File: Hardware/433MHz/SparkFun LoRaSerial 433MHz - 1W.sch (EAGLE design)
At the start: 96 parts, among them J1 QWIIC_RIGHT_ANGLE, J3 USB C, J4 JTAG, Q1 20V/0.2A/8MHz/1.2Ω/1Vth, Q2 20V/0.2A/8MHz/1.2Ω/1Vth, Q3 600mA/40V, Q4 600mA/40V, Q5 600mA/40V, Q6 600mA/40V, Q8 20V/4.2A/52mΩ/1.4W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

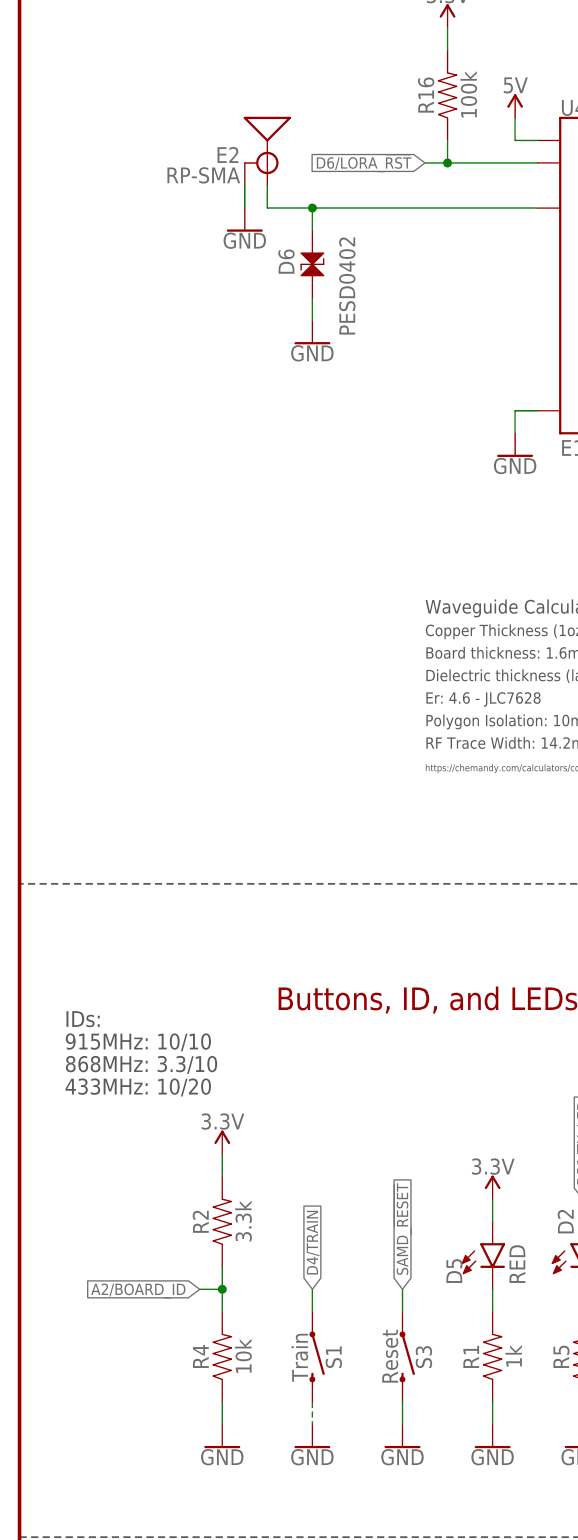
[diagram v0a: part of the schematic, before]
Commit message: Add 433MHz and 868MHz designs
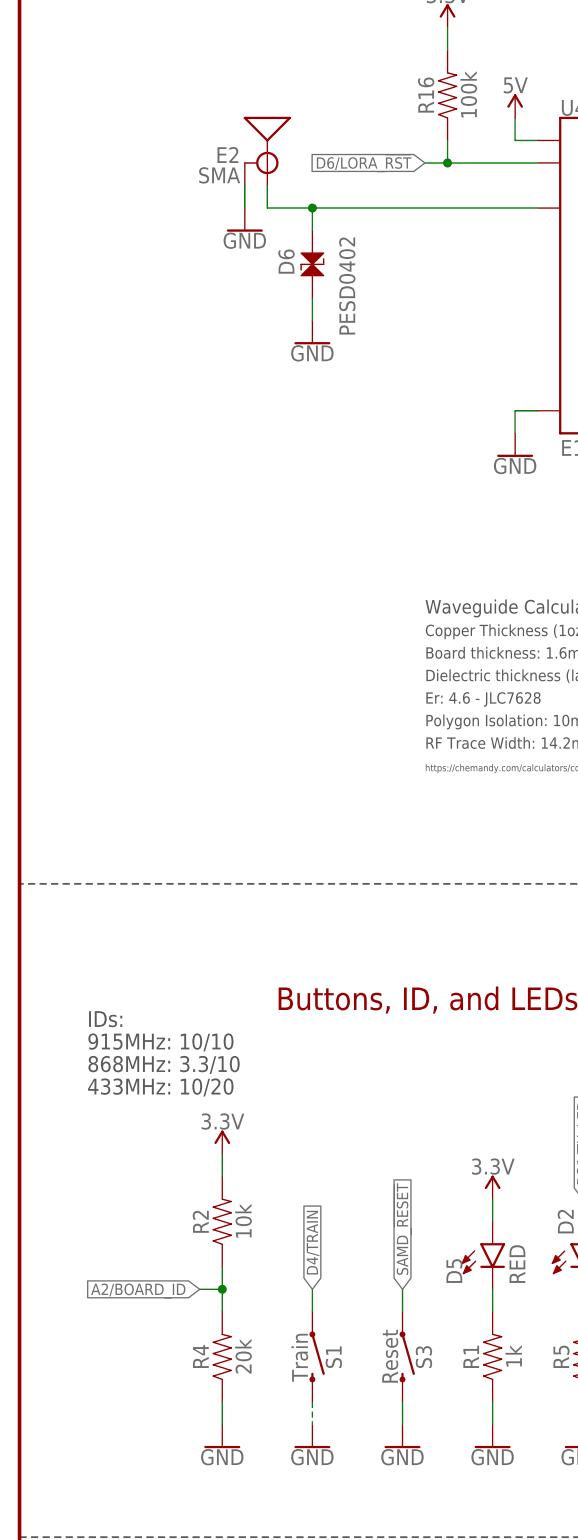
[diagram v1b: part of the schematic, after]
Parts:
- E2: value RP-SMA -> SMA; device SparkFun-RF:ANTENNA-SMA-GROUNDEDEDGE_RPSMA -> SparkFun-RF:ANTENNA-SMA-GROUNDEDEDGE_SMA
- R2: value 3.3k -> 10k; device SparkFun-Resistors:3.3KOHM-0603-1/10W-1% -> SparkFun-Resistors:10KOHM-0603-1/10W-1%
- R4: value 10k -> 20k; device SparkFun-Resistors:10KOHM-0603-1/10W-1% -> SparkFun-Resistors:20KOHM-0603-1/10W-1%
- U4: device SparkFun-RF:LORA-E19868MHZ -> SparkFun-RF:LORA-E19433MHZ
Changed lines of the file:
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@@
 <part name="LOGO4" library="SparkFun-Aesthetics" deviceset="OSHW-LOGO" device="MINI" value="OSHW-LOGOMINI"/>
 <part name="GND31" library="SparkFun-PowerSymbols" deviceset="GND" device=""/>
-<part name="U4" library="SparkFun-RF" deviceset="LORA-E19" device="868MHZ" value="E19-915M30S"/>
+<part name="U4" library="SparkFun-RF" deviceset="LORA-E19" device="433MHZ" value="E19-915M30S"/>
 <part name="R16" library="SparkFun-Resistors" deviceset="100KOHM" device="-0603-1/10W-1%" value="100k"/>
 <part name="SUPPLY12" library="SparkFun-PowerSymbols" deviceset="3.3V" device=""/>
@@
 <part name="SUPPLY13" library="SparkFun-PowerSymbols" deviceset="5V" device=""/>
 <part name="GND4" library="SparkFun-PowerSymbols" deviceset="GND" device=""/>
-<part name="R2" library="SparkFun-Resistors" deviceset="3.3KOHM" device="-0603-1/10W-1%" value="3.3k"/>
-<part name="R4" library="SparkFun-Resistors" deviceset="10KOHM" device="-0603-1/10W-1%" value="10k"/>
+<part name="R2" library="SparkFun-Resistors" deviceset="10KOHM" device="-0603-1/10W-1%" value="10k"/>
+<part name="R4" library="SparkFun-Resistors" deviceset="20KOHM" device="-0603-1/10W-1%" value="20k"/>
 <part name="SUPPLY7" library="SparkFun-PowerSymbols" deviceset="3.3V" device=""/>
 <part name="GND3" library="SparkFun-PowerSymbols" deviceset="GND" device=""/>
@@
 <part name="SUPPLY9" library="SparkFun-PowerSymbols" deviceset="3.3V" device=""/>
 <part name="JP9" library="SparkFun-Jumpers" deviceset="JUMPER-SMT_3_2-NC_TRACE" device="_SILK" package3d_urn="urn:adsk.eagle:package:39289/1" value="JUMPER-SMT_3_2-NC_TRACE_SILK"/>
-<part name="E2" library="SparkFun-RF" deviceset="ANTENNA-SMA-GROUNDED" device="EDGE_RPSMA" value="RP-SMA"/>
+<part name="E2" library="SparkFun-RF" deviceset="ANTENNA-SMA-GROUNDED" device="EDGE_SMA" value="SMA"/>
 <part name="S1" library="SparkFun-Switches" deviceset="MOMENTARY-SWITCH-SPST" device="-SMD-RIGHT-ANGLE" value="Train"/>
 <part name="GND9" library="SparkFun-PowerSymbols" deviceset="GND" device=""/>
@@
 <wire x1="88.9" y1="76.2" x2="88.9" y2="149.86" width="0.2032" layer="97" style="longdash"/>
 <wire x1="66.04" y1="0" x2="66.04" y2="76.2" width="0.2032" layer="97" style="longdash"/>
-<text x="5.08" y="134.62" size="1.778" layer="97" align="center-left">IDs:</text>
-<text x="5.08" y="132.08" size="1.778" layer="97" align="center-left">915MHz: 10/10</text>
-<text x="5.08" y="129.54" size="1.778" layer="97" align="center-left">868MHz: 3.3/10</text>
-<text x="5.08" y="127" size="1.778" layer="97" align="center-left">433MHz: 10/20</text>
+<text x="7.62" y="134.62" size="1.778" layer="97" align="center-left">IDs:</text>
+<text x="7.62" y="132.08" size="1.778" layer="97" align="center-left">915MHz: 10/10</text>
+<text x="7.62" y="129.54" size="1.778" layer="97" align="center-left">868MHz: 3.3/10</text>
+<text x="7.62" y="127" size="1.778" layer="97" align="center-left">433MHz: 10/20</text>
 </plain>
 <instances>
@@
 </sheet>
 </sheets>
-<errors>
-</errors>
 </schematic>
 </drawing>

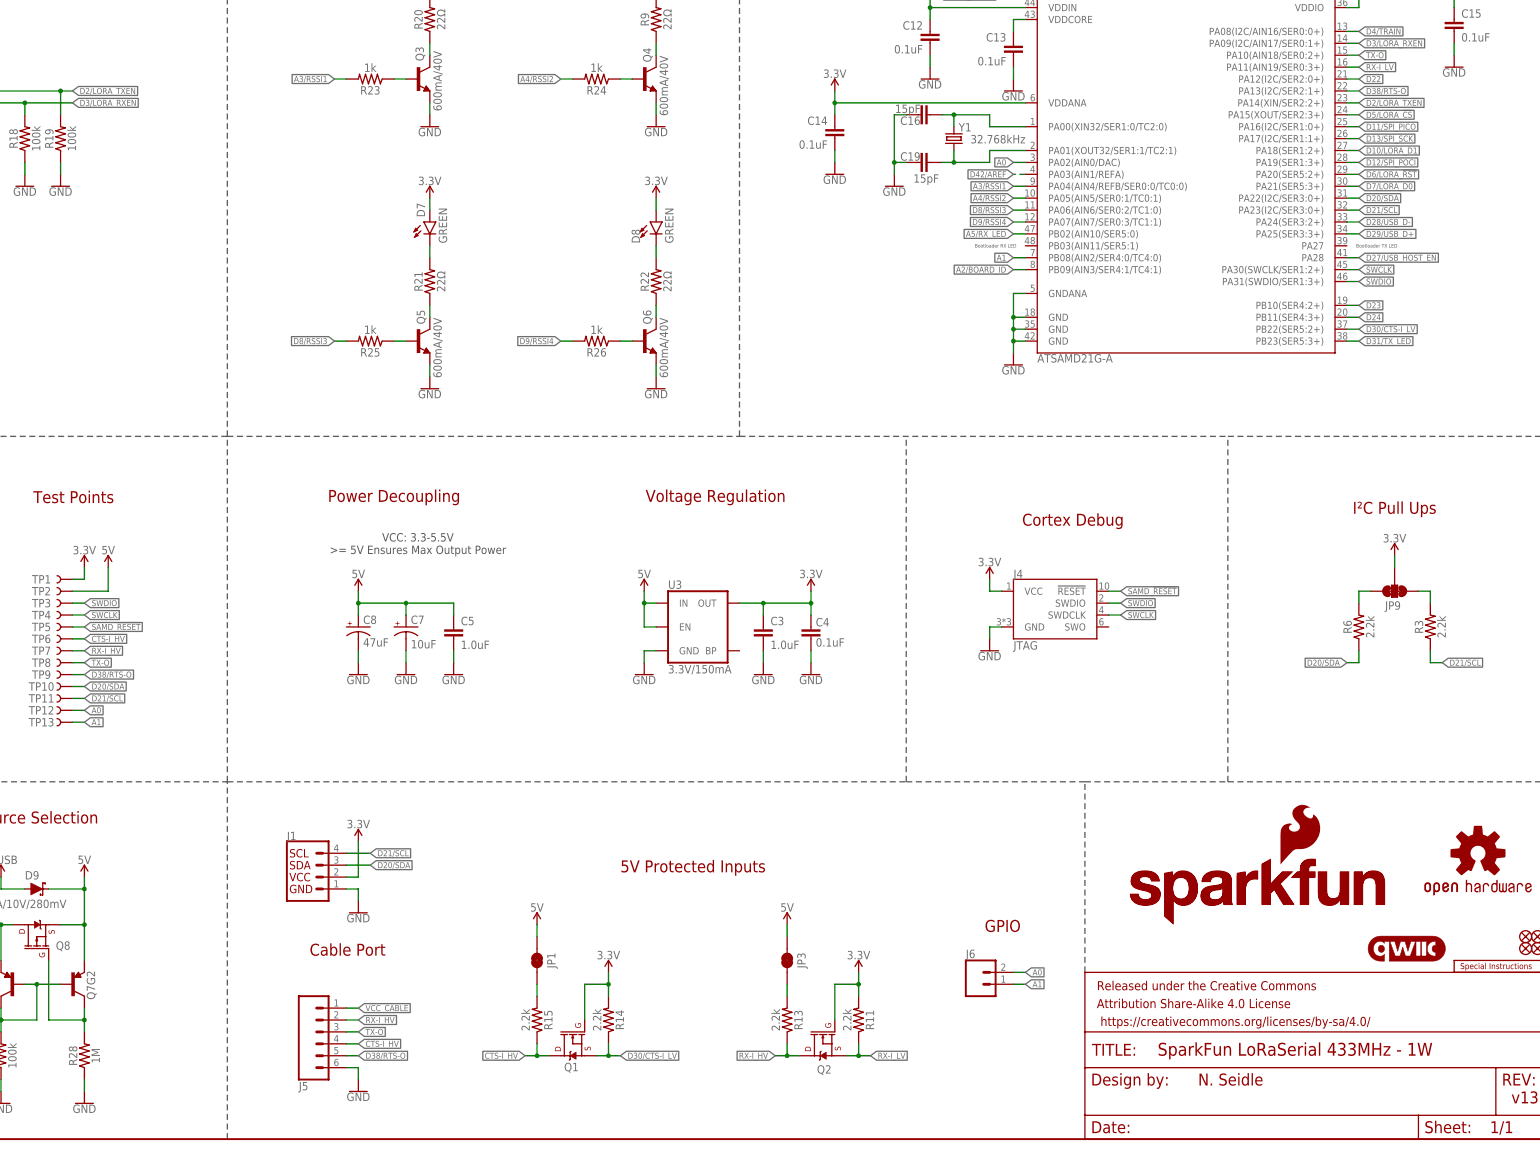
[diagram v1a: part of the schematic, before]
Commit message: Update schematics with flow control notes
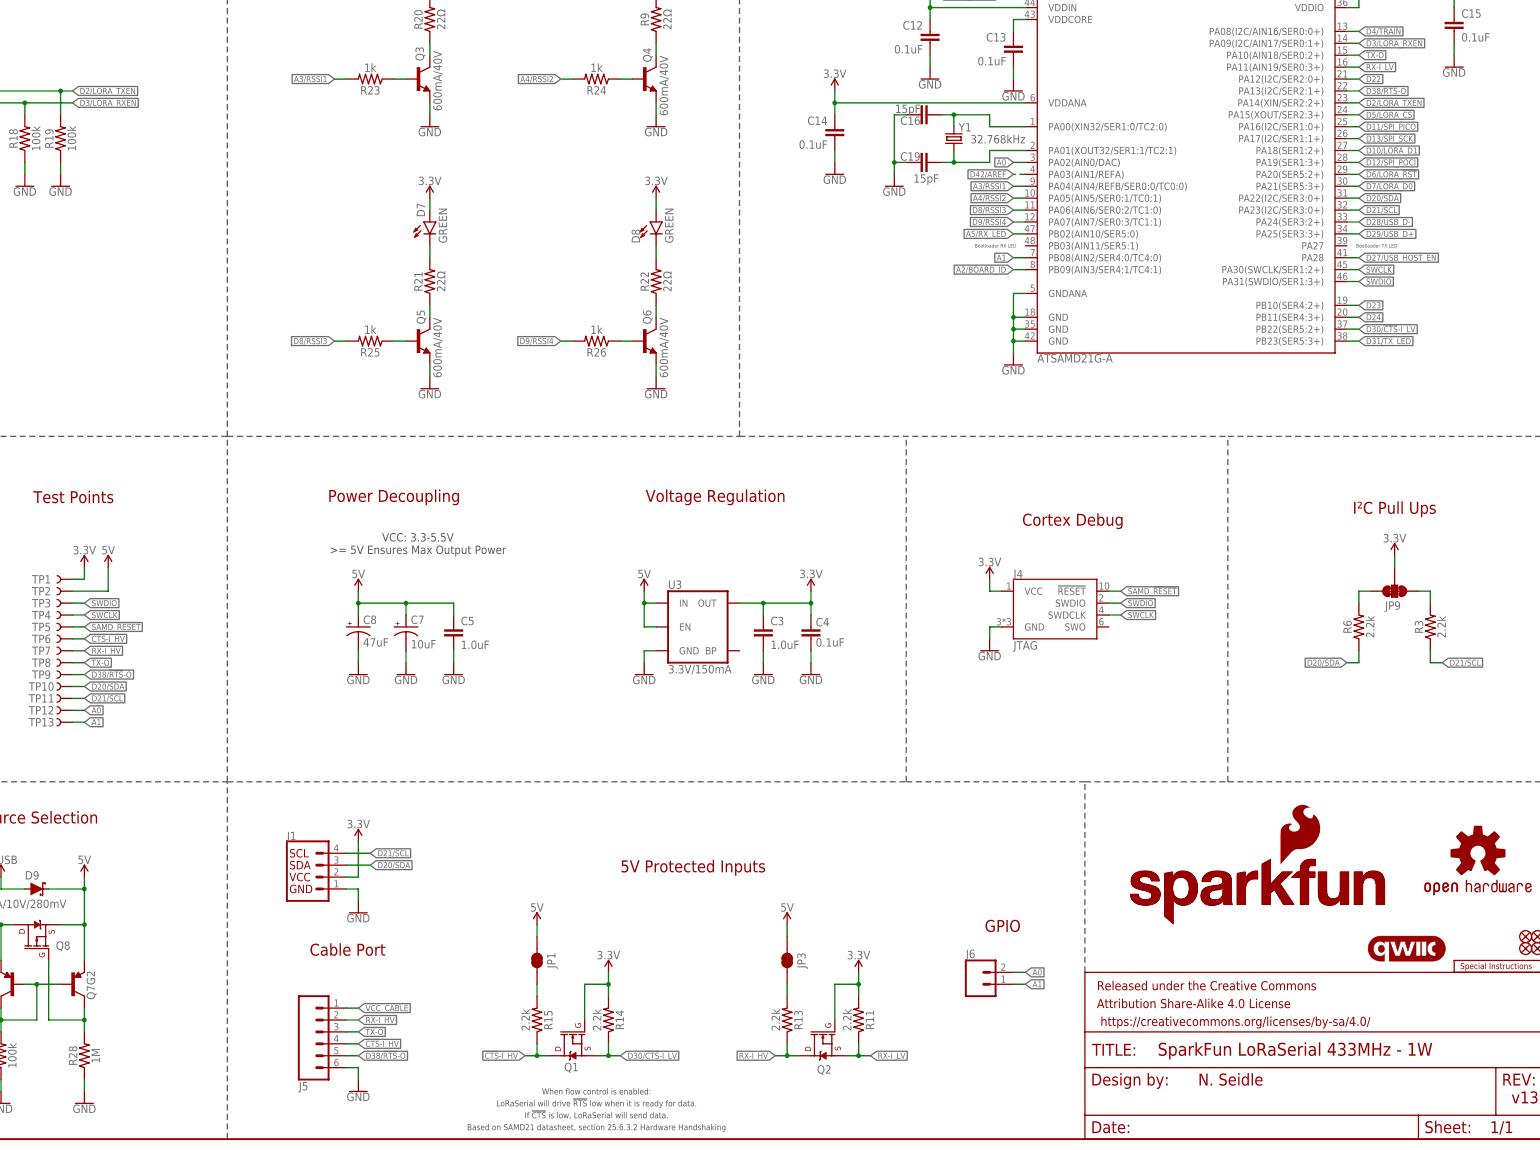
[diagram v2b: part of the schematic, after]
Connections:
- net CTS-I_HV renamed !CTS!-I_HV
- net D30/CTS-I_LV renamed D30/!CTS!-I_LV
- net D38/RTS-O renamed D38/!RTS!-O
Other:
- note added: "Based on SAMD21 datasheet, section 25.6.3.2 Hardware Handshaking"
- note added: "If !CTS! is low, LoRaSerial will send data."
- note added: "LoRaSerial will drive !RTS! low when it is ready for data."
- note added: "When flow control is enabled:"
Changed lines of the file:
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@@
 <text x="7.62" y="129.54" size="1.778" layer="97" align="center-left">868MHz: 3.3/10</text>
 <text x="7.62" y="127" size="1.778" layer="97" align="center-left">433MHz: 10/20</text>
+<text x="226.06" y="7.62" size="1.27" layer="97" font="vector" align="center">LoRaSerial will drive !RTS! low when it is ready for data.</text>
+<text x="226.06" y="5.08" size="1.27" layer="97" font="vector" align="center">If !CTS! is low, LoRaSerial will send data.</text>
+<text x="226.06" y="2.54" size="1.27" layer="97" font="vector" align="center">Based on SAMD21 datasheet, section 25.6.3.2 Hardware Handshaking</text>
+<text x="226.06" y="10.16" size="1.27" layer="97" font="vector" align="center">When flow control is enabled:</text>
 </plain>
 <instances>
@@
 </segment>
 </net>
-<net name="D30/CTS-I_LV" class="0">
+<net name="D30/!CTS!-I_LV" class="0">
 <segment>
 <pinref part="U2" gate="G$1" pin="PB22(SER5:2+)"/>
@@
 </segment>
 </net>
-<net name="D38/RTS-O" class="0">
+<net name="D38/!RTS!-O" class="0">
 <segment>
 <pinref part="U2" gate="G$1" pin="PA13(I2C/SER2:1+)"/>
@@
 </segment>
 </net>
-<net name="CTS-I_HV" class="0">
+<net name="!CTS!-I_HV" class="0">
 <segment>
 <label x="175.26" y="20.32" size="1.27" layer="95" font="vector" xref="yes"/>
